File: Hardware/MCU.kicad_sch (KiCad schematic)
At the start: 27 parts, among them J1 Conn_ARM_SWD_TagConnect_TC203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, SW1 SW_SPDT, SW2 SW_Push, U1 STM32G431CBTx, Y1 Crystal_GND24

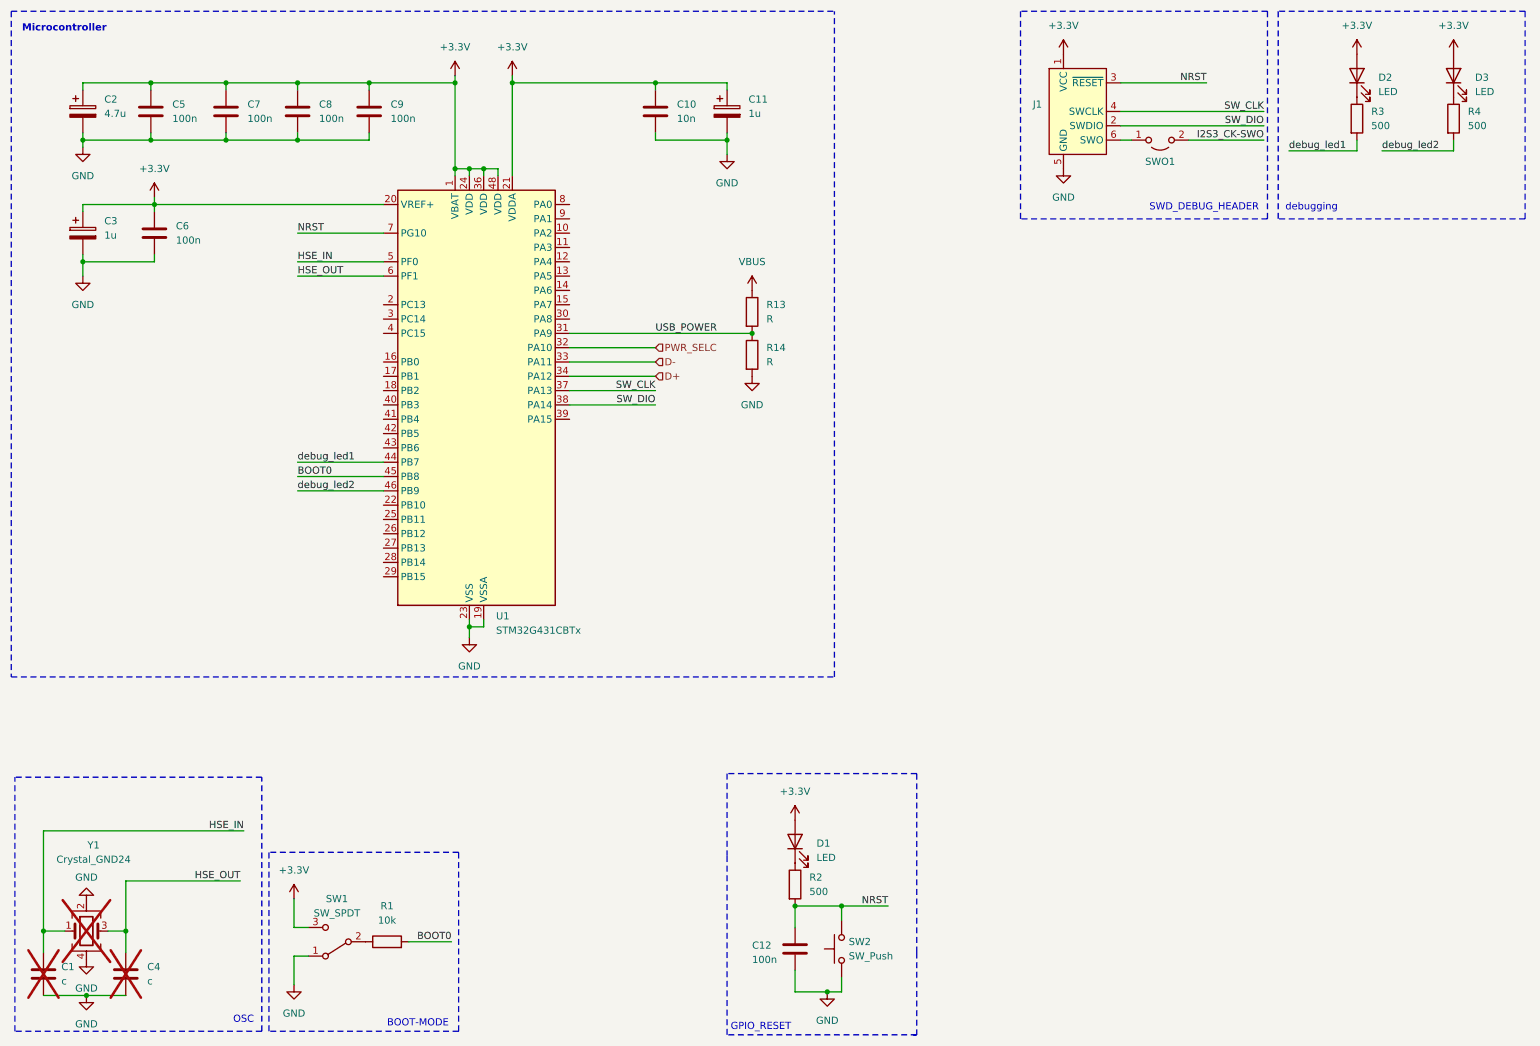
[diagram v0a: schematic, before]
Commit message: CODEC schematics
Missing mic ins and all audio outputs.
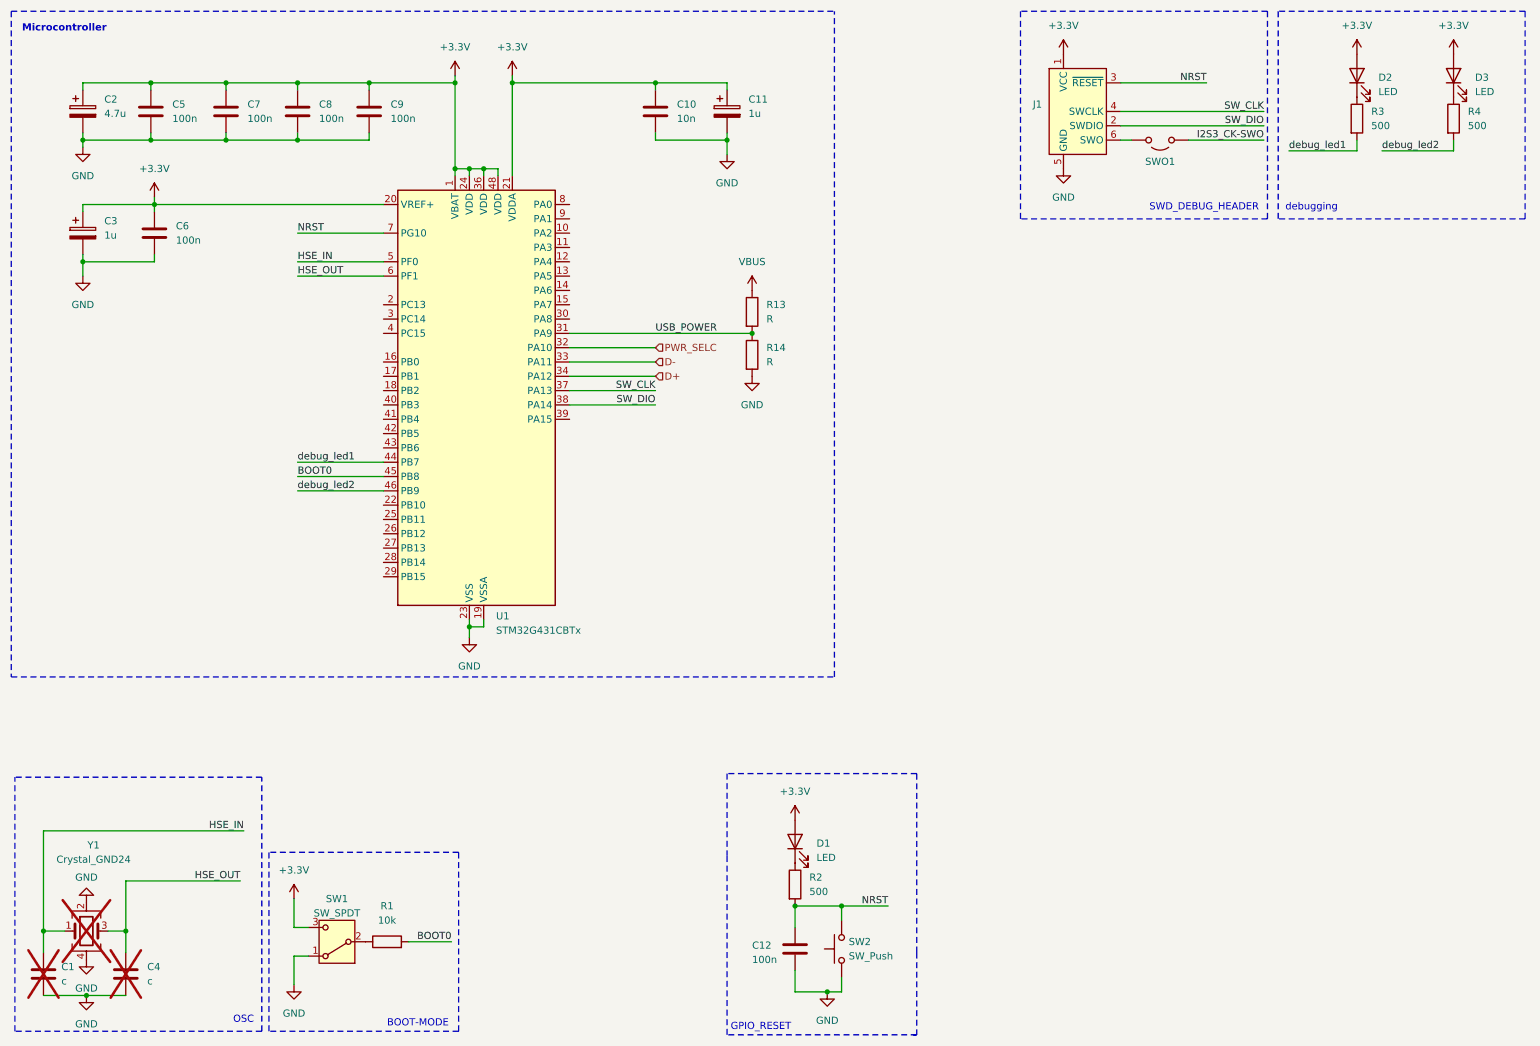
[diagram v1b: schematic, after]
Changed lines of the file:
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@@
 			)
 		)
-		(property "Description" ""
+		(property "Description" "Unpolarized capacitor"
 			(at 52.07 31.75 0)
 			(effects
@@
 			)
 		)
-		(property "Description" ""
+		(property "Description" "Power symbol creates a global label with name \"+3.3V\""
 			(at 64.135 171.45 0)
 			(effects
@@
 			)
 		)
-		(property "Description" ""
+		(property "Description" "Unpolarized capacitor"
 			(at 128.27 31.75 0)
 			(effects
@@
 			)
 		)
-		(property "Description" ""
+		(property "Description" "Power symbol creates a global label with name \"+3.3V\""
 			(at 153.035 157.48 0)
 			(effects
@@
 			)
 		)
-		(property "Description" ""
+		(property "Description" "Light emitting diode"
 			(at 252.73 25.4 0)
 			(effects
@@
 			)
 		)
-		(property "Description" ""
+		(property "Description" "Unpolarized capacitor"
 			(at 39.37 53.34 0)
 			(effects
@@
 			)
 		)
-		(property "Description" ""
+		(property "Description" "Power symbol creates a global label with name \"GND\" , ground"
 			(at 200.66 41.91 0)
 			(effects
@@
 			)
 		)
-		(property "Description" ""
+		(property "Description" "Power symbol creates a global label with name \"GND\" , ground"
 			(at 140.97 39.37 0)
 			(effects
@@
 			)
 		)
-		(property "Description" ""
+		(property "Description" "Power symbol creates a global label with name \"+3.3V\""
 			(at 269.875 21.59 0)
 			(effects
@@
 			)
 		)
-		(property "Description" ""
+		(property "Description" "STMicroelectronics Arm Cortex-M4 MCU, 128KB flash, 32KB RAM, 170 MHz, 1.71-3.6V, 38 GPIO, LQFP48"
 			(at 95.25 83.82 0)
 			(effects
@@
 			)
 		)
-		(property "Description" ""
+		(property "Description" "Polarized capacitor"
 			(at 26.67 31.75 0)
 			(effects
@@
 			)
 		)
-		(property "Description" ""
+		(property "Description" "Resistor"
 			(at 80.645 179.07 0)
 			(effects
@@
 			)
 		)
-		(property "Description" ""
+		(property "Description" "Power symbol creates a global label with name \"GND\" , ground"
 			(at 27.305 182.245 0)
 			(effects
@@
 			)
 		)
-		(property "Description" ""
+		(property "Description" "Power symbol creates a global label with name \"+3.3V\""
 			(at 252.73 21.59 0)
 			(effects
@@
 			)
 		)
-		(property "Description" ""
+		(property "Description" "Unpolarized capacitor"
 			(at 64.77 31.75 0)
 			(effects
@@
 			)
 		)
-		(property "Description" ""
+		(property "Description" "Power symbol creates a global label with name \"GND\" , ground"
 			(at 158.75 187.96 0)
 			(effects
@@
 			)
 		)
-		(property "Description" ""
+		(property "Description" "Unpolarized capacitor"
 			(at 77.47 31.75 0)
 			(effects
@@
 			)
 		)
-		(property "Description" ""
+		(property "Description" "Polarized capacitor"
 			(at 26.67 53.34 0)
 			(effects
@@
 			)
 		)
-		(property "Description" ""
+		(property "Description" "Power symbol creates a global label with name \"GND\" , ground"
 			(at 64.135 186.69 0)
 			(effects
@@
 			)
 		)
-		(property "Description" ""
+		(property "Description" "Power symbol creates a global label with name \"GND\" , ground"
 			(at 26.67 38.1 0)
 			(effects
@@
 			)
 		)
-		(property "Description" ""
+		(property "Description" "Unpolarized capacitor"
 			(at 153.035 180.34 0)
 			(effects
@@
 			)
 		)
-		(property "Description" ""
+		(property "Description" "Power symbol creates a global label with name \"+3.3V\""
 			(at 200.66 21.59 0)
 			(effects
@@
 			)
 		)
-		(property "Description" ""
+		(property "Description" "Power symbol creates a global label with name \"GND\" , ground"
 			(at 95.25 125.095 0)
 			(effects
@@
 			)
 		)
-		(property "Description" ""
+		(property "Description" "Resistor"
 			(at 153.035 168.91 0)
 			(effects
@@
 			)
 		)
-		(property "Description" ""
+		(property "Description" "Power symbol creates a global label with name \"+3.3V\""
 			(at 39.37 46.99 0)
 			(effects
@@
 			)
 		)
-		(property "Description" ""
+		(property "Description" "Switch, single pole double throw"
 			(at 71.755 179.07 0)
 			(effects
@@
 			)
 		)
-		(property "Description" ""
+		(property "Description" "Power symbol creates a global label with name \"GND\" , ground"
 			(at 27.305 188.595 0)
 			(effects
@@
 			)
 		)
-		(property "Description" ""
+		(property "Description" "Light emitting diode"
 			(at 153.035 161.29 0)
 			(effects
@@
 			)
 		)
-		(property "Description" ""
+		(property "Description" "Power symbol creates a global label with name \"+3.3V\""
 			(at 102.87 25.4 0)
 			(effects
@@
 			)
 		)
-		(property "Description" ""
+		(property "Description" "Resistor"
 			(at 252.73 33.02 0)
 			(effects
@@
 			)
 		)
-		(property "Description" ""
+		(property "Description" "Unpolarized capacitor"
 			(at 19.685 184.785 0)
 			(effects
@@
 			)
 		)
-		(property "Description" ""
+		(property "Description" "Unpolarized capacitor"
 			(at 38.735 31.75 0)
 			(effects
@@
 			)
 		)
-		(property "Description" ""
+		(property "Description" "Light emitting diode"
 			(at 269.875 25.4 0)
 			(effects
@@
 			)
 		)
-		(property "Description" ""
+		(property "Description" "Power symbol creates a global label with name \"+3.3V\""
 			(at 92.71 25.4 0)
 			(effects
@@
 			)
 		)
-		(property "Description" ""
+		(property "Description" "Resistor"
 			(at 269.875 33.02 0)
 			(effects
@@
 			)
 		)
-		(property "Description" ""
+		(property "Description" "Power symbol creates a global label with name \"GND\" , ground"
 			(at 145.415 78.74 0)
 			(effects
@@
 			)
 		)
-		(property "Description" ""
+		(property "Description" "Polarized capacitor"
 			(at 140.97 31.75 0)
 			(effects
@@
 			)
 		)
-		(property "Description" ""
+		(property "Description" "Unpolarized capacitor"
 			(at 34.29 184.785 0)
 			(effects
@@
 			)
 		)
-		(property "Description" ""
+		(property "Description" "Power symbol creates a global label with name \"GND\" , ground"
 			(at 27.305 172.085 0)
 			(effects
@@
 			)
 		)
-		(property "Description" ""
+		(property "Description" "Power symbol creates a global label with name \"GND\" , ground"
 			(at 26.67 60.96 0)
 			(effects

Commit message: added I2S and I2C to the stm32
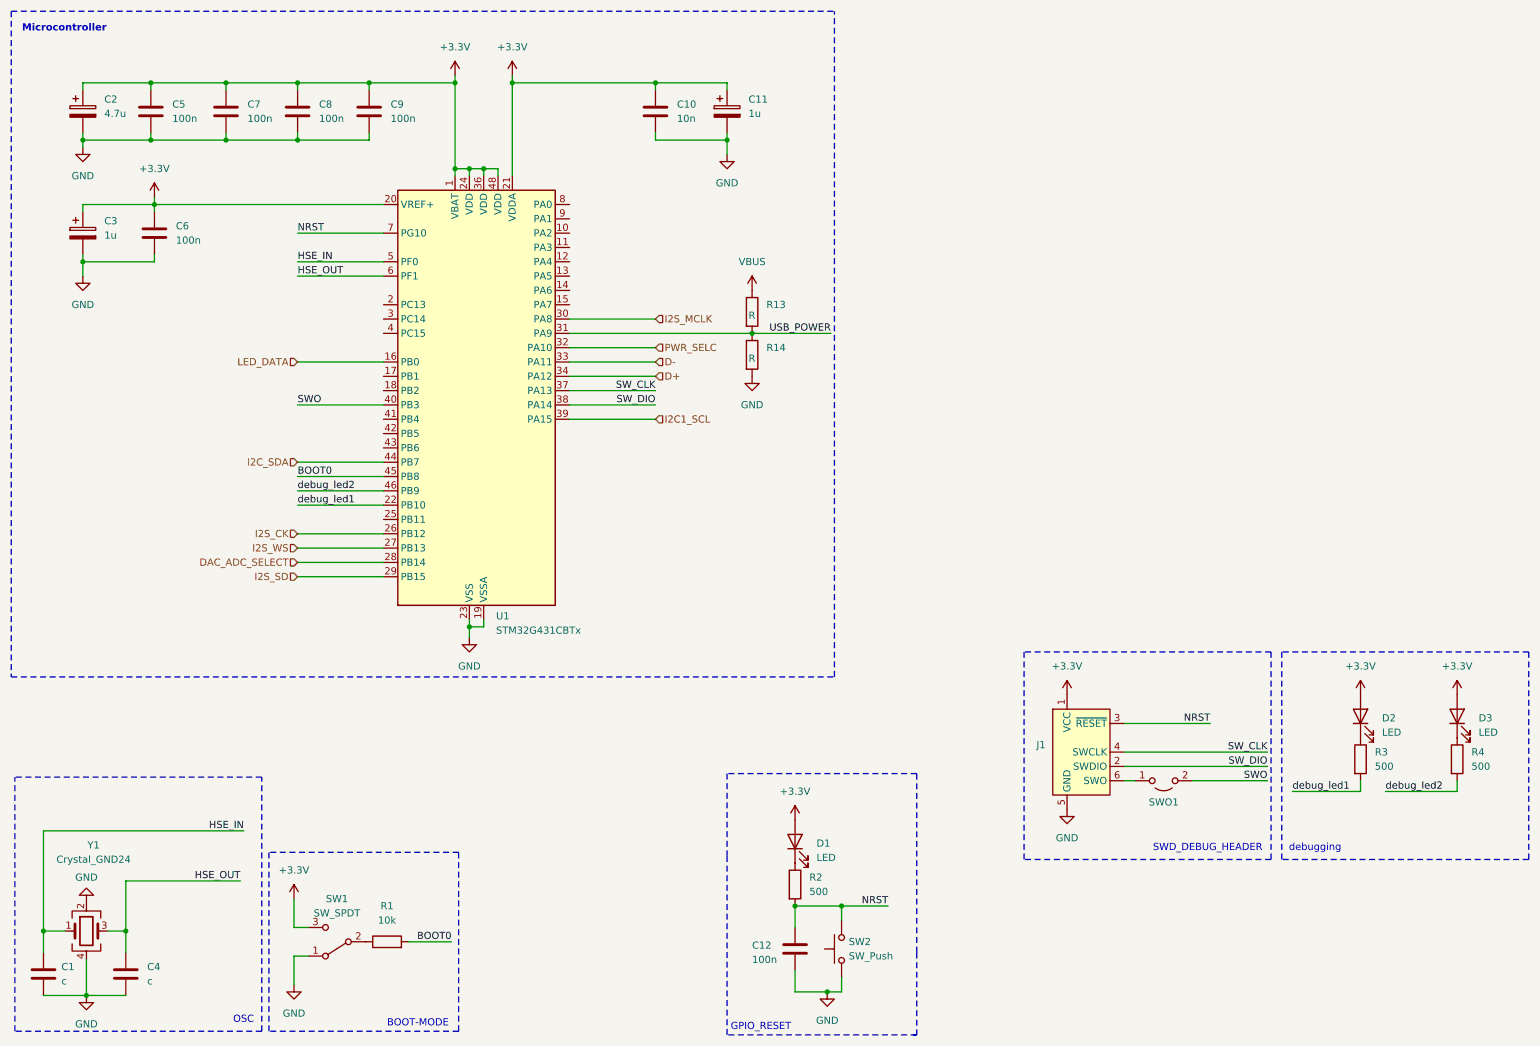
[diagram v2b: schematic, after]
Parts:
- C1, C4, Y1: now fitted
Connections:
- net I2S3_CK-SWO is gone; now on net SWO: SWO1.2 (B)
- net debug_led1: now also U1.22 (PB10); no longer U1.44 (PB7)
- net LED_DATA: now reaches U1.16 (PB0)
- net I2S_CK: now reaches U1.26 (PB12)
- net I2S_WS: now reaches U1.27 (PB13)
- net DAC_ADC_SELECT: now reaches U1.28 (PB14)
- net I2S_SD: now reaches U1.29 (PB15)
- net I2S_MCLK: now reaches U1.30 (PA8)
- net I2C1_SCL: now reaches U1.39 (PA15)
- net SWO: now reaches U1.40 (PB3)
- new net I2C_SDA: U1.44 (PB7)
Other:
- moved on the sheet: D2, D3, J1, R3, R4
